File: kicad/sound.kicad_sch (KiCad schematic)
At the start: 16 parts, among them J4 Speaker, U17 LM386, U3 AY-3-8912, U33 GAL16V8

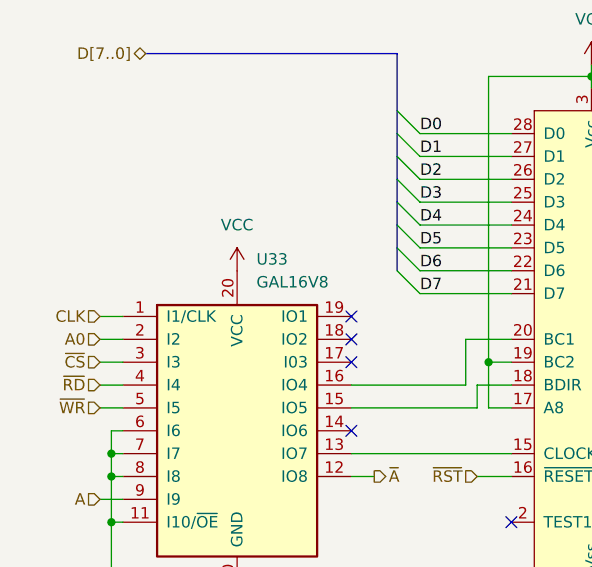
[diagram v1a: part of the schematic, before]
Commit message: hw: add RC to /RD for CF for increased compatibility
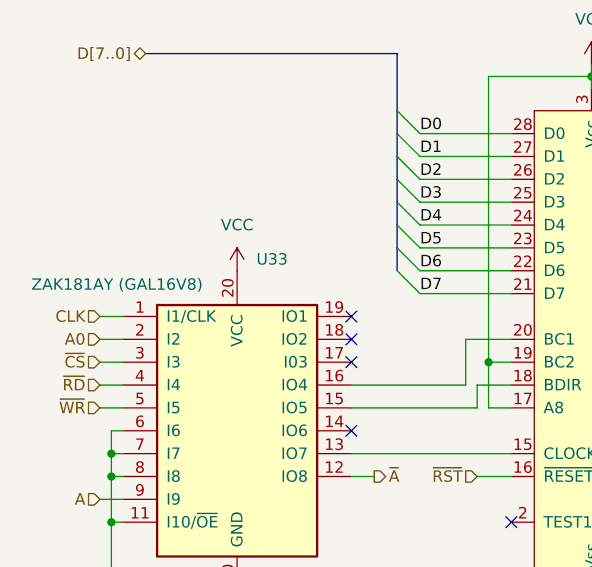
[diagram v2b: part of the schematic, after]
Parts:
- U33: value GAL16V8 -> ZAK181AY (GAL16V8)
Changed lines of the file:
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@@
 		(on_board yes)
 		(dnp no)
-		(fields_autoplaced yes)
 		(property "Reference" "U33"
 			(at 93.5833 88.9 0)
@@
 			)
 		)
-		(property "Value" "GAL16V8"
-			(at 93.5833 91.44 0)
+		(property "Value" "ZAK181AY (GAL16V8)"
+			(at 68.58 91.694 0)
 			(effects
 				(font
